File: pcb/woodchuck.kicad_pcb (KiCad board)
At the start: 2 copper layers, 28 parts, among them IC201 u-blox_CAM-M8Q, IC601 MS5611-01BA03, J401 JSTA-4, P101 CONN_01X02, P401 SWD, P402 USB_OTG, U301 Radiometrix_MTX2, U401 STM32F072CBT6

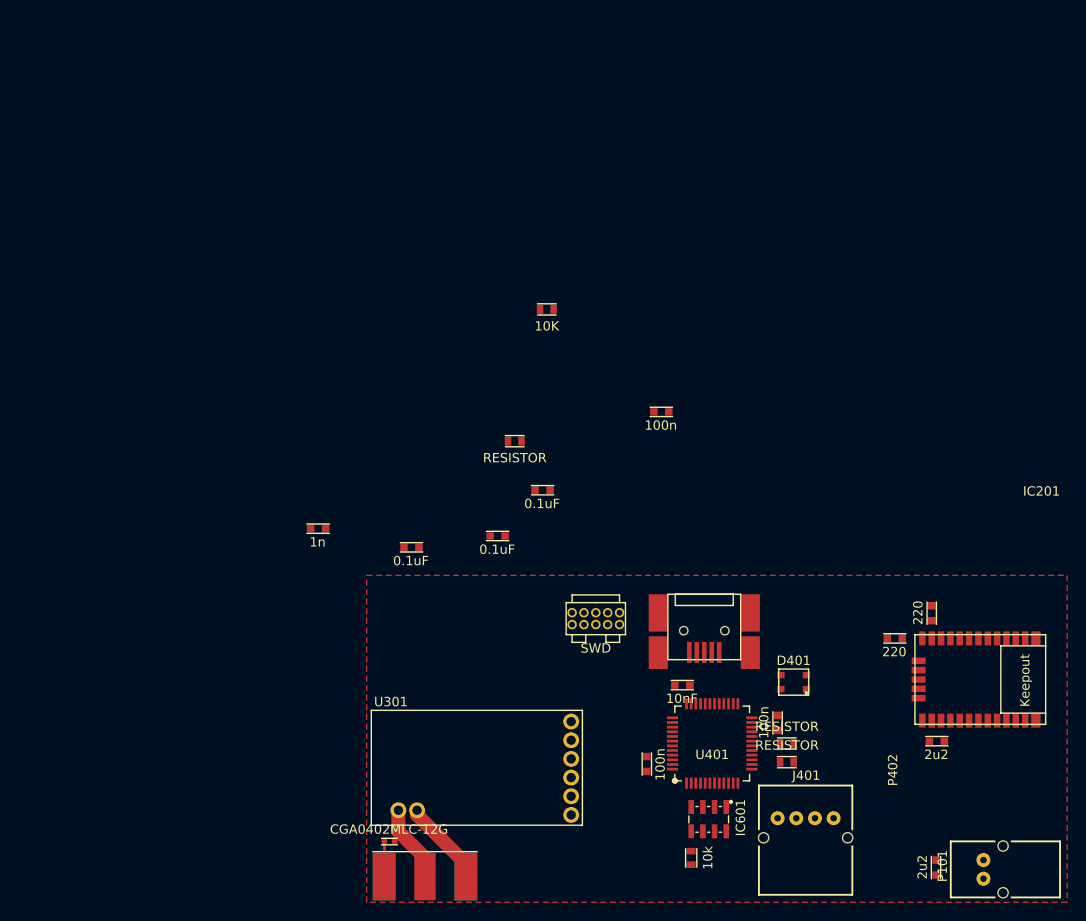
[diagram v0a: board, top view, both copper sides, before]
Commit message: Worked on PCB layout
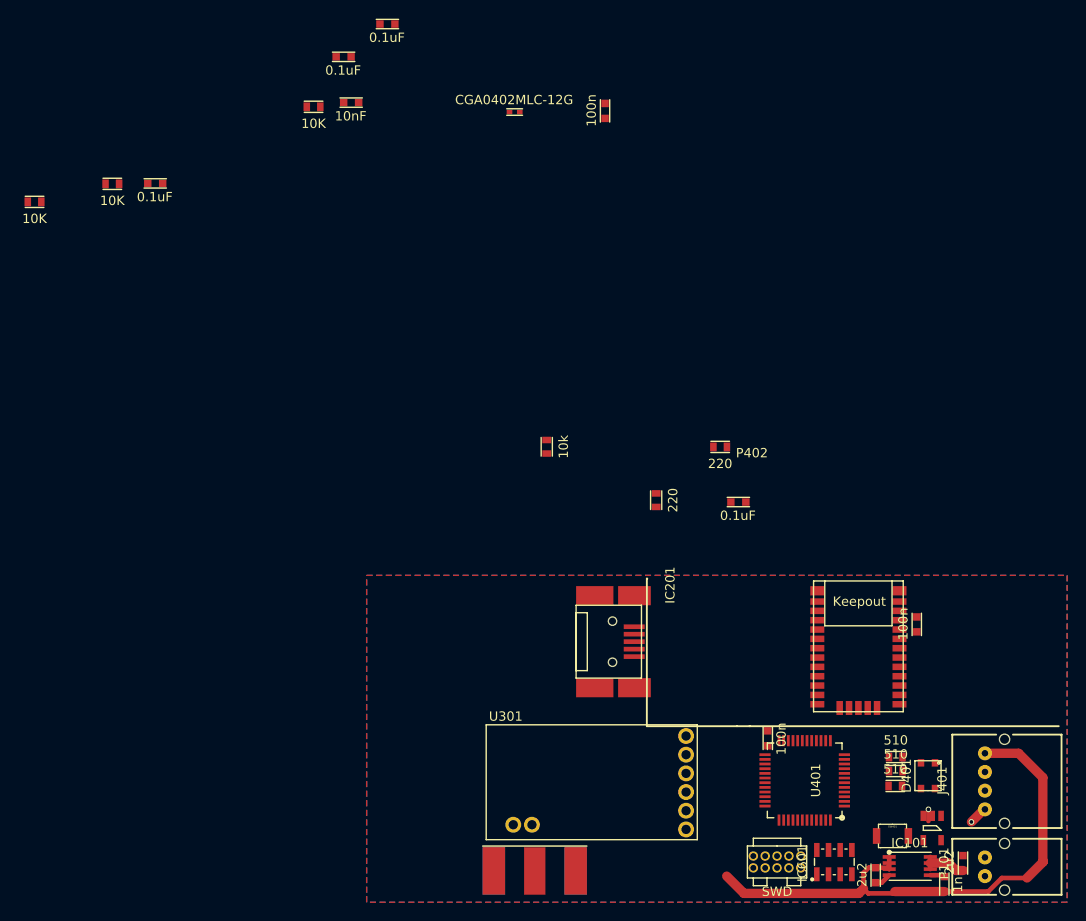
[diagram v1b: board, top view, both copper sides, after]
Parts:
- added C1: 0.1uF, Woodchuck:C0603, F.Cu at (126.6, 58.0)
- added IC1: 24AA01, agg:SOT-23-5, F.Cu at (210.6, 127.0)
- added IC101: ADP3335, Woodchuck:MSOP8, F.Cu at (205.9, 130.2)
- added R1: 10K, Woodchuck:0603, F.Cu at (144.3, 49.8)
- added R2: 10K, Woodchuck:0603, F.Cu at (114.4, 60.0)
- added SW401: SPST, Woodchuck:B3U-1000P_switch, F.Cu at (206.3, 127.9)
- D401: value LED_RCBG -> LED_RABG
- R201, R202: footprint Woodchuck:C0603 -> Woodchuck:0603
- R401, R402, R403: value RESISTOR -> 510
- moved D301 79.2 mm to (166.4, 50.4)
- moved C102 78.2 mm to (211.8, 133.8), turned to 90 degrees
- moved C401 71.7 mm to (147.5, 49.4)
- moved C301 68.1 mm to (175.5, 49.5)
- moved C402 56.1 mm to (151.4, 41.0)
- moved R402 54.0 mm to (206.7, 121.0), turned to 180 degrees
- moved C404 51.1 mm to (146.7, 44.5)
- moved R404 48.4 mm to (122.8, 58.1)
- moved R601 46.7 mm to (169.3, 86.2)
- moved C201 35.7 mm to (208.9, 104.5), turned to 270 degrees
- moved P401 32.5 mm to (191.4, 130.1)
- moved R202 28.8 mm to (181.0, 92.0), turned to 90 degrees
- moved R201 28.3 mm to (187.8, 86.2), turned to 0 degrees
- moved C403 26.0 mm to (189.0, 92.2)
- moved J401 17.6 mm to (216.2, 119.0), turned to 270 degrees
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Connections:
- C101 pad 1: Earth -> GND
- D401 pad 2: GND -> (no net)
- IC201 pad 2: Net-(IC201-Pad2) -> (no net)
- IC201 pad 28: Net-(IC201-Pad28) -> (no net)
- IC201 pad 29: Net-(IC201-Pad29) -> (no net)
- IC201 pad 3: Net-(IC201-Pad3) -> (no net)
- IC201 pad 30: Net-(IC201-Pad30) -> (no net)
- IC201 pad 6: Net-(IC201-Pad6) -> (no net)
- IC201 pad 7: Net-(IC201-Pad7) -> (no net)
- IC601 pad 8: /barometer/BARO_SCK -> /microcontroller/BARO_CLK
- P101 pad 1: Earth -> GND
- P401 pad 6: Net-(P401-Pad6) -> (no net)
- P401 pad 7: Net-(P401-Pad7) -> (no net)
- P401 pad 8: Net-(P401-Pad8) -> (no net)
- P402 pad 1: Net-(P402-Pad1) -> (no net)
- P402 pad 4: Net-(P402-Pad4) -> (no net)
- R401 pad 1: Net-(D401-Pad1) -> Net-(D401-Pad3)
- R403 pad 1: Net-(D401-Pad3) -> Net-(D401-Pad1)
- U401 pad 1: Net-(U401-Pad1) -> (no net)
- U401 pad 10: Net-(U401-Pad10) -> (no net)
- U401 pad 11: Net-(U401-Pad11) -> (no net)
- U401 pad 12: /microcontroller/GPS_FROM_MCU -> /GPS/GPS_FROM_MCU
- U401 pad 13: /microcontroller/GPS_TO_MCU -> /GPS/GPS_TO_MCU
- U401 pad 17: Net-(U401-Pad17) -> (no net)
- U401 pad 18: Net-(U401-Pad18) -> (no net)
- U401 pad 19: Net-(U401-Pad19) -> (no net)
- U401 pad 2: Net-(U401-Pad2) -> (no net)
- U401 pad 20: Net-(U401-Pad20) -> (no net)
- U401 pad 25: Net-(U401-Pad25) -> (no net)
- U401 pad 26: Net-(U401-Pad26) -> /Radio/MTX2_P0
- U401 pad 27: Net-(U401-Pad27) -> /Radio/MTX2_P1
- U401 pad 28: /microcontroller/RADIO_TX -> /Radio/MTX2_TXD
- U401 pad 29: Net-(U401-Pad29) -> (no net)
- U401 pad 3: Net-(U401-Pad3) -> (no net)
- U401 pad 30: /microcontroller/RADIO_EN -> /Radio/MTX2_EN/PGM
- U401 pad 31: Net-(U401-Pad31) -> (no net)
- U401 pad 38: /microcontroller/BARO_CS_N -> /barometer/BARO_CS
- U401 pad 4: Net-(U401-Pad4) -> (no net)
- U401 pad 40: /microcontroller/BARO_MISO -> /barometer/BARO_MISO
- U401 pad 41: /microcontroller/BARO_MOSI -> /barometer/BARO_MOSI
- U401 pad 45: Net-(U401-Pad45) -> (no net)
- U401 pad 46: Net-(U401-Pad46) -> (no net)
- U401 pad 5: Net-(U401-Pad5) -> (no net)
- U401 pad 6: Net-(U401-Pad6) -> (no net)
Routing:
- net +3V3: track 0.00 -> 58.9 mm
- net Net-(A301-Pad1): track 9.55 -> 0.00 mm
- net GND: track 10.6 -> 3.79 mm, vias 0 -> 1
- net +BATT: track 0.00 -> 5.13 mm
- net Net-(C102-Pad2): track 0.00 -> 1.56 mm
- net (no net): track 0.00 -> 1.25 mm, vias 0 -> 1
- added copper zone on B.Cu, net GND
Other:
- net class Default: clearance 0.2 -> 0.1
- rule trace_clearance: 0.2 -> 0.1

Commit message: Continued routing PCB
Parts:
- moved R1 99.1 mm to (207.9, 125.8), turned to 90 degrees
- moved C301 80.6 mm to (184.2, 129.6), turned to 180 degrees
- moved R601 55.5 mm to (203.6, 129.9), turned to 180 degrees
- moved C403 33.9 mm to (191.2, 126.0), turned to 90 degrees
- moved R201 27.5 mm to (196.2, 112.5)
- moved R202 26.6 mm to (196.2, 113.8), turned to 0 degrees
- moved R404 5.90 mm to (128.6, 59.3)
- moved P402 1.85 mm to (177.2, 106.7)
- moved SW401 1.26 mm to (205.1, 127.5)
- moved D401 1.16 mm to (210.2, 120.3)
- moved IC601 0.36 mm to (198.3, 132.2)
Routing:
- net /microcontroller/SWDIO: track 0.00 -> 8.32 mm
- net /microcontroller/SWCLK: track 0.00 -> 4.46 mm
- net GND: track 3.79 -> 7.64 mm, vias 1 -> 2
- net /barometer/BARO_CS: track 0.00 -> 3.05 mm
- net +3V3: track 58.9 -> 61.1 mm
- net (no net): track 1.25 -> 0.00 mm, vias 1 -> 0
